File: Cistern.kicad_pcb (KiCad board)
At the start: 2 copper layers, 47 x 80 mm, 18 parts, among them J2 Gauge Stepper, J3 Power Connector, Q1 BD244C, Q2 Gauge Calibration, SW1 WiFi reset, SW2 Water Sensor, U1 ULN2003A, U3 Boost Converter (5->20 V)

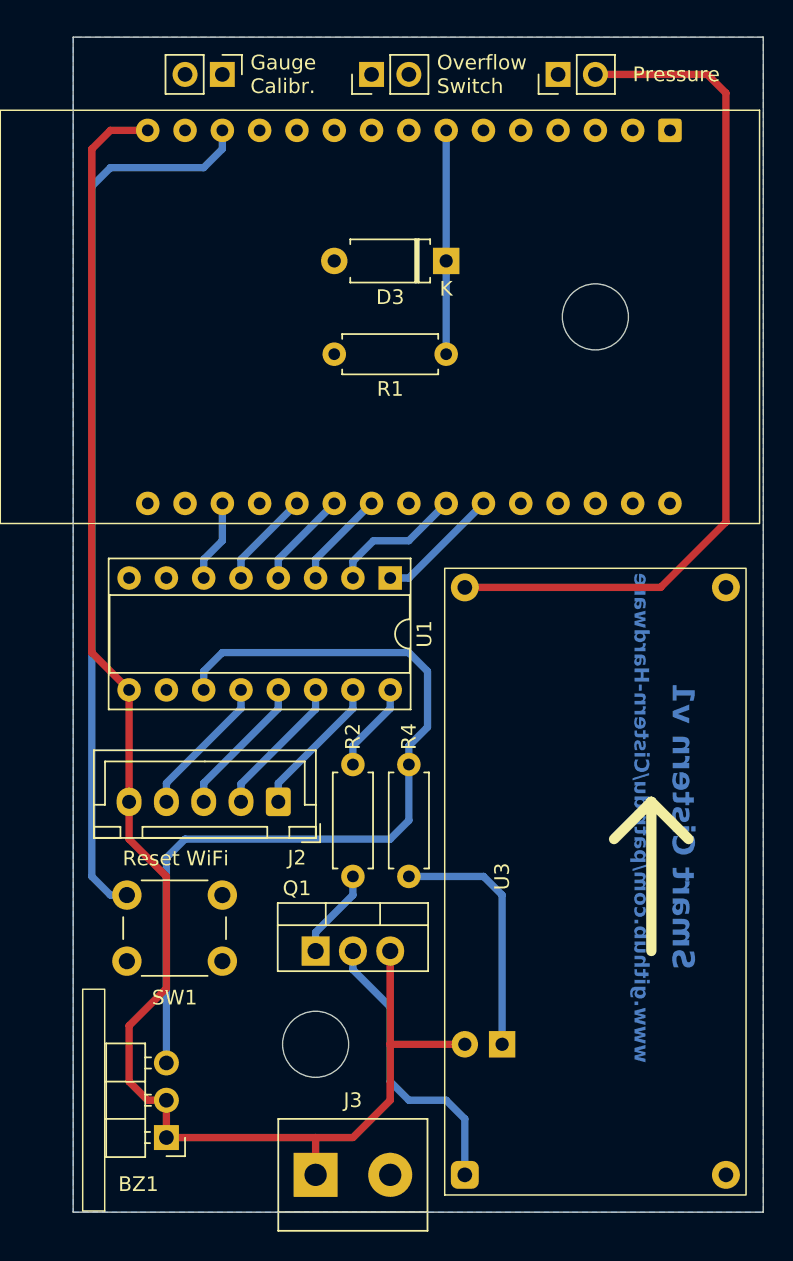
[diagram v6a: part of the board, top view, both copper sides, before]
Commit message: Replacing individual pins with GPIO header
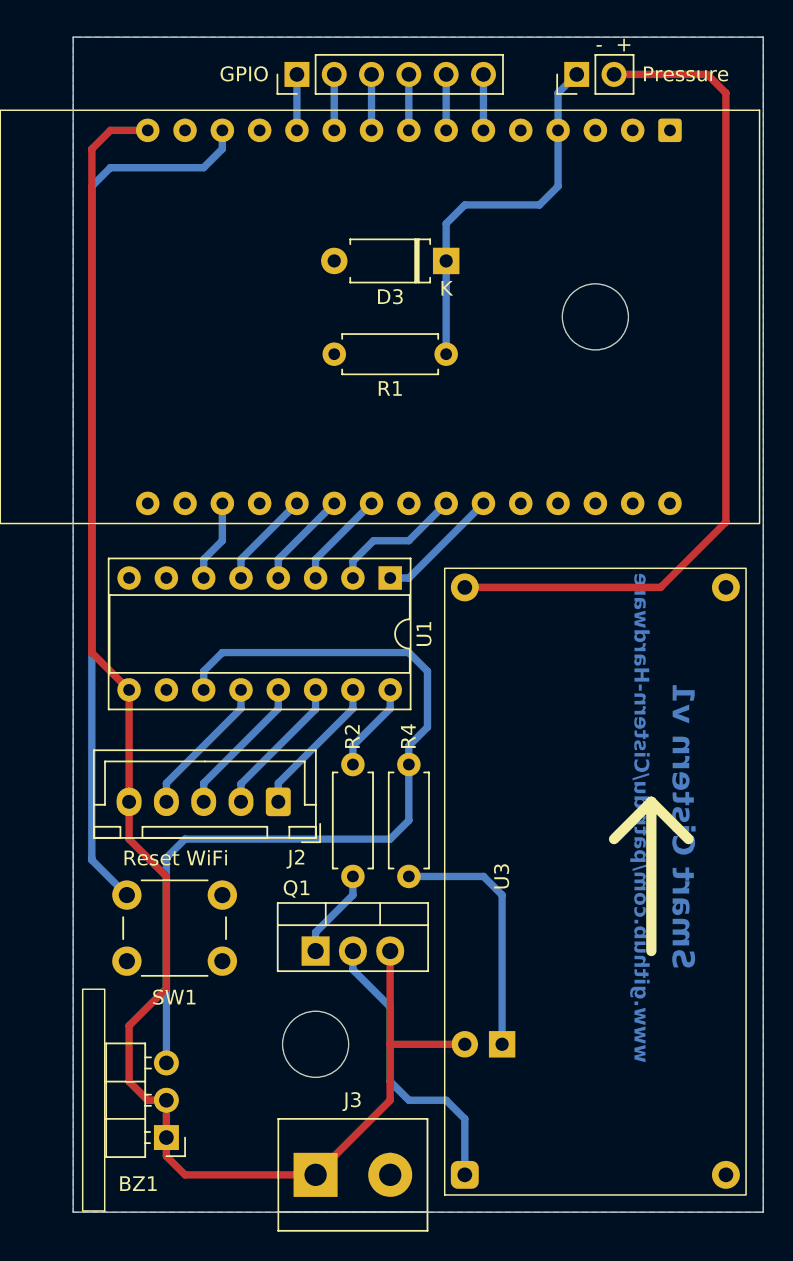
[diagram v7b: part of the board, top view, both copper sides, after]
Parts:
- removed Q2: Gauge Calibration, Connector_PinHeader_2.54mm:PinHeader_1x02_P2.54mm_Vertical
- removed SW2: Water Sensor, Connector_PinHeader_2.54mm:PinHeader_1x02_P2.54mm_Vertical
- added J1: GPIO, Connector_PinHeader_2.54mm:PinHeader_1x06_P2.54mm_Vertical, F.Cu at (100.3, 47.0)
- moved D2 1.27 mm to (119.4, 47.0)
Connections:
- MCU1 pad 11: unconnected-(MCU1-GPIO14-Pad11) -> Net-(J1-Pin_1)
- MCU1 pad 17: Net-(MCU1-GPIO22) -> unconnected-(MCU1-GPIO22-Pad17)
- MCU1 pad 4: unconnected-(MCU1-GPIO34-Pad4) -> Net-(D2-K)
- MCU1 pad 6: unconnected-(MCU1-GPIO32-Pad6) -> Net-(J1-Pin_6)
- MCU1 pad 7: Net-(D2-K) -> Net-(J1-Pin_5)
- MCU1 pad 8: unconnected-(MCU1-GPIO25-Pad8) -> Net-(J1-Pin_4)
- MCU1 pad 9: unconnected-(MCU1-GPIO26-Pad9) -> Net-(J1-Pin_3)
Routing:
- net Net-(D2-K): track 15.2 -> 25.7 mm
- net Net-(J1-Pin_6): track 0.00 -> 3.81 mm
- net Net-(J1-Pin_5): track 0.00 -> 3.81 mm
- net Net-(J1-Pin_4): track 0.00 -> 3.81 mm
- net Net-(J1-Pin_3): track 0.00 -> 3.81 mm
- net Net-(J1-Pin_2): track 0.00 -> 3.81 mm
- net Net-(J1-Pin_1): track 0.00 -> 3.81 mm
- net Net-(D2-A): track 58.2 -> 57.0 mm
- net Net-(MCU1-GPIO13): track 61.1 -> 60.5 mm
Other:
- board text added: "- +"
- board text added: "GPIO"
- board text removed: "Gauge Calibr."
- board text removed: "Overflow Switch"

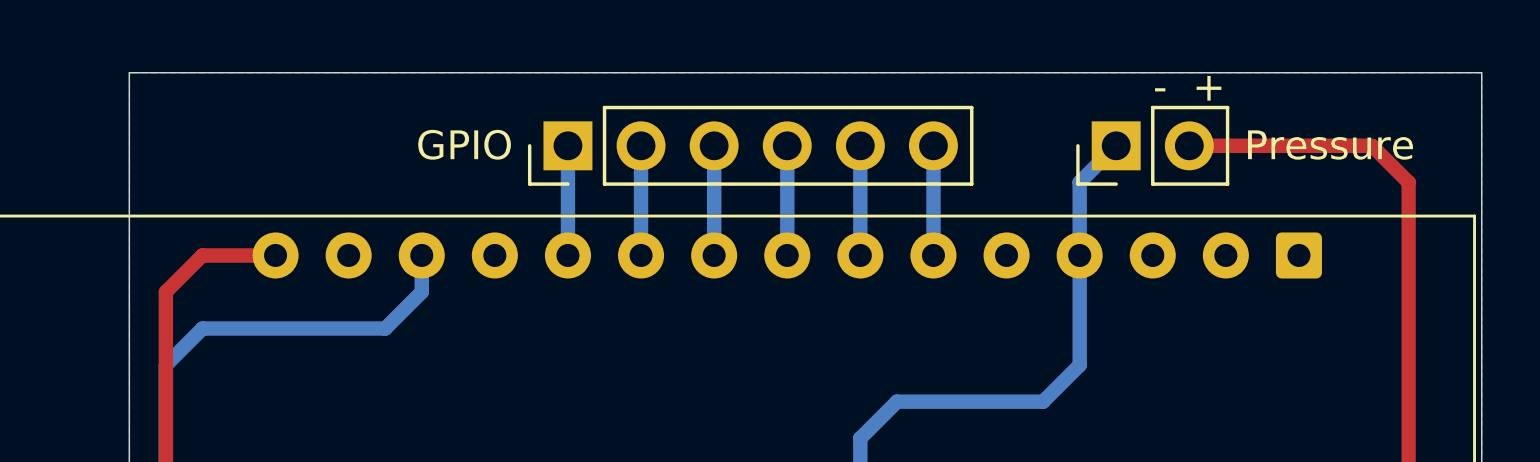
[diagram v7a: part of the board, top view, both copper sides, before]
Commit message: Adding GND header
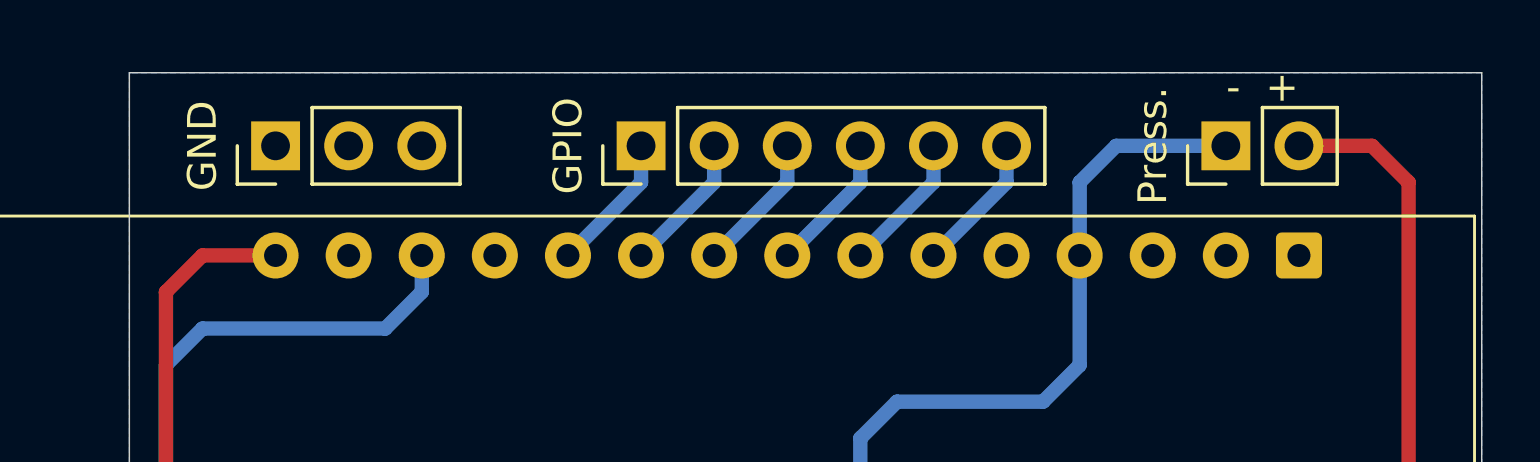
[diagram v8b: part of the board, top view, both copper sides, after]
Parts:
- added J4: GND, Connector_PinHeader_2.54mm:PinHeader_1x03_P2.54mm_Vertical, F.Cu at (90.2, 47.0)
- moved D2 3.81 mm to (123.2, 47.0)
- moved J1 2.54 mm to (102.9, 47.0)
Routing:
- net Net-(D2-K): track 25.7 -> 29.5 mm
- net Net-(D2-A): track 57.0 -> 53.2 mm
- net Net-(J1-Pin_5): track 3.81 -> 4.86 mm
- net Net-(J1-Pin_3): track 3.81 -> 4.86 mm
- net Net-(J1-Pin_1): track 3.81 -> 4.86 mm
- net Net-(J1-Pin_6): track 3.81 -> 4.86 mm
- net Net-(J1-Pin_4): track 3.81 -> 4.86 mm
- net Net-(J1-Pin_2): track 3.81 -> 4.86 mm
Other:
- board text added: "GND"
- board text added: "Press."
- board text removed: "Pressure"
